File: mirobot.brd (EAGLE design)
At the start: 73.9 x 40.6 mm, 26 parts, among them IC1 ULN2003AN, IC2 ULN2003AN, IC3 ATMEGA 328, Q2 16M, X1 5_PIN_STEPPER, X2 5_PIN_STEPPER

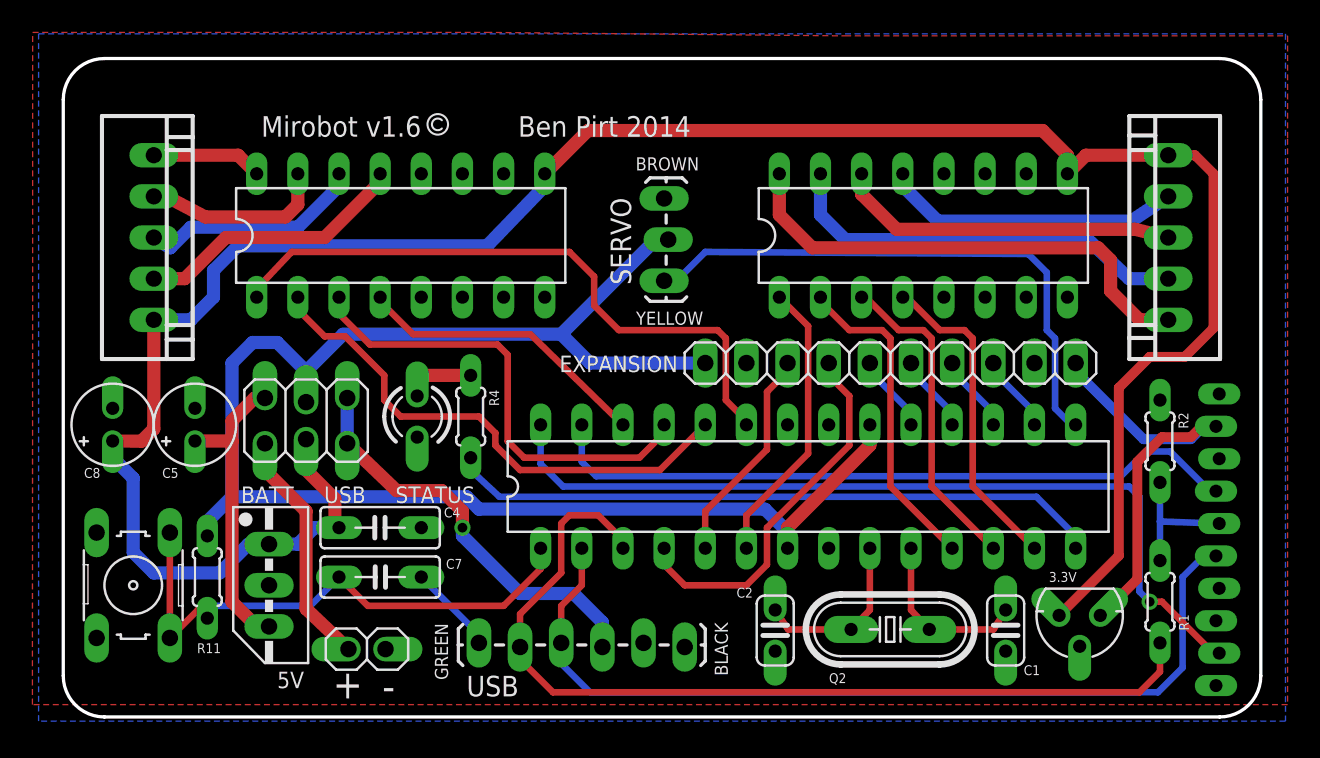
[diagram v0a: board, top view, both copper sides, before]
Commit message: Re-worked board to use the Arduino Pro Mini form factor
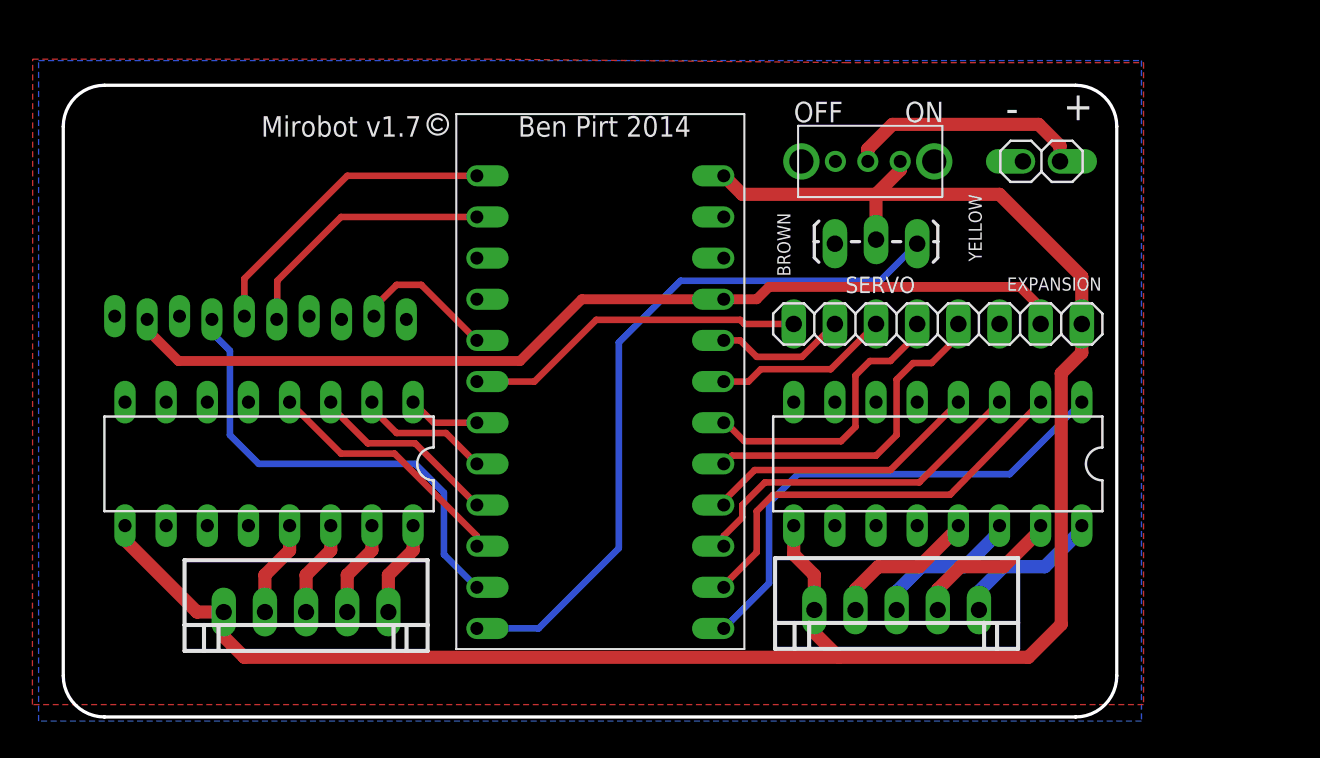
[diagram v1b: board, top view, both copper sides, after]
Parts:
- removed 3.3V: 3.3V, Child-Friendly-Parts:78LXX
- removed 5V: (no value), v-reg:78MXXS
- removed C1, C2: 22p, Child-Friendly-Parts:C025-024X044
- removed C4, C7: 100n, Child-Friendly-Parts:C050-025X075
- removed C5, C8: 100u, Child-Friendly-Parts:E2-5
- removed IC3: ATMEGA 328, atmel:DIL28-3
- removed JP5: PowerSelect, Child-Friendly-Parts:2X03
- removed Q2: 16M, Child-Friendly-Parts:HC49/S
- removed R1: 470R, Child-Friendly-Parts:0204/5
- removed R11: 10k, Child-Friendly-Parts:0204/5
- removed R2, R4: 1k, Child-Friendly-Parts:0204/5
- removed S1: Reset, switch-omron:B3F-10XX
- removed STATUS: (no value), Child-Friendly-Parts:LED3MM
- removed USB: (no value), SparkFun-Connectors:1X06_LOCK_LONGPADS
- added U$2: ARDUINO_PRO_MINI, custom:ARDUINO_PRO_MINI
- added U$3: SPDT_SLIDE_SWITCH, custom:SPDT_SLIDE_SWITCH
- EXPANSION: device pinhead:1X10 -> pinhead:1X08
- moved U$1 61.4 mm to (20.1, 40.4), turned to 0 degrees
- moved X2 58.0 mm to (23.9, 22.2), turned to 180 degrees
- moved JP6 51.4 mm to (69.3, 50.0), turned to 180 degrees
- moved X1 51.3 mm to (60.3, 22.4), turned to 180 degrees
- moved IC2 42.8 mm to (21.6, 31.4), turned to 180 degrees
- moved IC1 36.0 mm to (62.9, 31.4), turned to 180 degrees
- moved SERVO 15.8 mm to (61.6, 45.0), turned to 180 degrees
- moved EXPANSION 3.79 mm to (62.9, 40.0)
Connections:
- removed net +5V: EXPANSION.10, IC3.20, IC3.7, JP5.3, R11.2, SERVO.2
- removed net EXT_RESET: C4.2, USB.1
- removed net N$12: IC2.1, IC3.6
- removed net N$13: IC1.1, IC3.23
- removed net N$14: IC1.2, IC3.24
- removed net N$15: IC1.3, IC3.25
- removed net N$16: IC2.2, IC3.11
- removed net N$17: IC2.3, IC3.12
- removed net N$18: IC2.4, IC3.13
- removed net N$19: R1.2, R2.2, U$1.RX
- removed net N$20: R4.1, STATUS.A
- removed net N$5: IC1.4, IC3.26
- removed net N$7: C2.2, IC3.9, Q2.2
- removed net PB2: EXPANSION.3, IC3.16
- removed net PB3: EXPANSION.4, IC3.17
- removed net PB4: EXPANSION.5, IC3.18
- removed net PB5: EXPANSION.6, IC3.19
- removed net PD2: EXPANSION.7, IC3.4
- removed net RESET: C4.1, IC3.1, R11.1, S1.1, S1.2
- removed net STATUS: IC3.14, R4.2
- removed net USBVCC: JP5.1, JP5.2, USB.4
- removed net V+: 3.3V.IN, 5V.IN, C7.2, C8.+, IC1.9, IC2.9, JP5.4, X1.5, X2.5
- removed net VCC: 5V.OUT, C5.+, JP5.5
- new net MOTOR1_1: IC1.1, U$2.D10
- new net MOTOR1_2: IC1.2, U$2.MOSI
- new net MOTOR1_3: IC1.3, U$2.MISO
- new net MOTOR1_4: IC1.4, U$2.SCK
- new net MOTOR2_1: IC2.1, U$2.D4
- new net MOTOR2_2: IC2.2, U$2.D5
- new net MOTOR2_3: IC2.3, U$2.D6
- new net MOTOR2_4: IC2.4, U$2.D7
- new net PC0: EXPANSION.4, U$2.A0
- new net PC1: EXPANSION.5, U$2.A1
- new net PC2: EXPANSION.6, U$2.A2
- new net PC3: EXPANSION.7, U$2.A3
- net +3V3: now also EXPANSION.2, U$2.VCC; no longer 3.3V.OUT, EXPANSION.1
- net GND: now also EXPANSION.3, U$2.GND, U$2.GND2, U$3.GND1, U$3.GND2; no longer 3.3V.GND, 5V.GND, C1.1, C2.1, C5.-, C7.1, C8.-, EXPANSION.2, EXPANSION.9, IC3.22, IC3.8, R2.1, S1.3, S1.4, STATUS.K, USB.6
- net N$6: now also JP6.1, U$3.COMMON; no longer C1.2, IC3.10, Q2.1
- net NREADY: now also U$2.D2; no longer IC3.28
- net PD3: now also U$2.D3; no longer IC3.5
- net RXD: now also U$2.RXI; no longer IC3.2, USB.3
- net SERVO: now also U$2.D9; no longer IC3.15
- net TXD: now also U$1.RX, U$2.TXO; no longer IC3.3, R1.1, USB.2
- net VSS: now also EXPANSION.1, IC1.9, IC2.9, SERVO.2, U$2.RAW, U$3.SW2, X1.5, X2.5; no longer JP5.6, JP6.1
- net WIFI_RESET: now also U$2.D8; no longer IC3.27
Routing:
- net V+: track 144.6 -> 0.00 mm
- net VSS: track 14.9 -> 124.8 mm
- net +5V: track 100.3 -> 0.00 mm
- net NREADY: track 52.6 -> 8.88 mm, vias 1 -> 0
- net STATUS: track 40.5 -> 0.00 mm
- net N$13: track 39.6 -> 0.00 mm
- net RXD: track 55.7 -> 16.3 mm
- net TXD: track 57.2 -> 19.3 mm
- net RESET: track 34.5 -> 0.00 mm
- net N$14: track 32.5 -> 0.00 mm
- net +3V3: track 27.7 -> 60.0 mm
- net MOTOR1_1: track 0.00 -> 30.8 mm
- net N$15: track 29.0 -> 0.00 mm
- net MOTOR1_2: track 0.00 -> 25.9 mm
- net USBVCC: track 25.5 -> 0.00 mm, vias 1 -> 0
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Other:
- board size 73.9 x 40.6 mm -> 65 x 39 mm
- board text added: "Mirobot v1.7"
- board text added: "OFF"
- board text added: "ON"
- board text removed: "BATT"
- board text removed: "BLACK"
- board text removed: "GREEN"
- board text removed: "Mirobot v1.6"
- board text removed: "USB"

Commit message: Fully routed board to be used for the early bird units
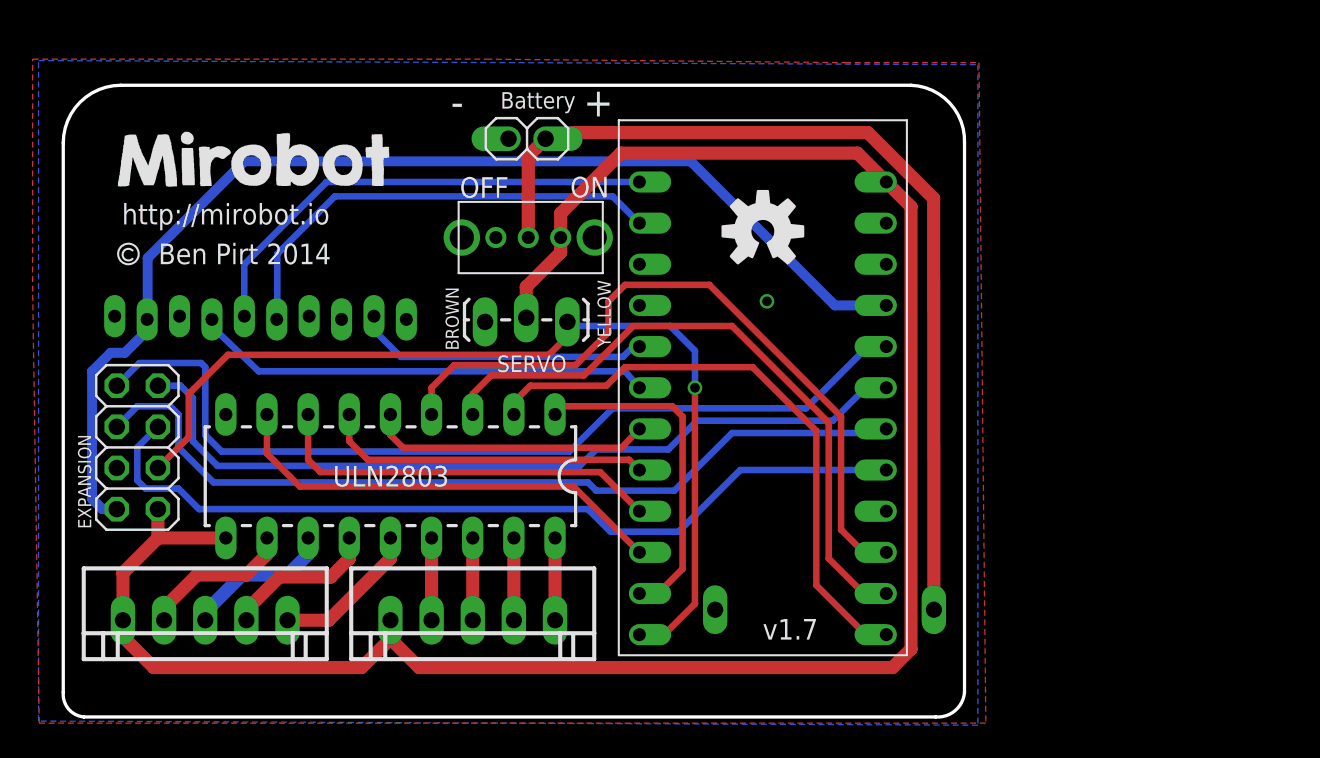
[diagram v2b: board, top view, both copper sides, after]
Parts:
- removed IC1, IC2: ULN2003AN, uln-udn:DIL16
- added LOGO1: OSHW-LOGOM, SparkFun-Aesthetics:OSHW-LOGO-M
- added U$4: BATTERY_PACK, custom:BATTERY_PACK
- added U$5: (no value), custom:LOGO
- added ULN2803: (no value), SparkFun-PowerIC:DIL18
- EXPANSION: device pinhead:1X08 -> pinhead:2X04
- moved EXPANSION 50.0 mm to (13.5, 32.4), turned to 90 degrees
- moved JP6 31.8 mm to (37.5, 51.4)
- moved X1 26.2 mm to (34.2, 21.7)
- moved SERVO 22.1 mm to (40.0, 40.1)
- moved U$3 21.5 mm to (37.6, 45.3)
- moved U$2 10.0 mm to (52.1, 36.1)
- moved X2 6.24 mm to (17.7, 21.7)
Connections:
- removed net N$10: IC2.14, X2.3
- removed net N$11: IC2.13, X2.4
- removed net PD3: EXPANSION.8, U$2.D3
- new net N$5: ULN2803.14, X2.1
- new net N$7: ULN2803.13, X2.2
- net GND: now also EXPANSION.4, U$4.GND, ULN2803.9; no longer EXPANSION.3, IC1.5, IC1.6, IC1.7, IC1.8, IC2.5, IC2.6, IC2.7, IC2.8
- net MOTOR1_1: now also U$2.D8, ULN2803.1; no longer IC1.1, U$2.D10
- net MOTOR1_2: now also U$2.D10, ULN2803.2; no longer IC1.2, U$2.MOSI
- net MOTOR1_3: now also U$2.MOSI, ULN2803.3; no longer IC1.3, U$2.MISO
- net MOTOR1_4: now also U$2.MISO, ULN2803.4; no longer IC1.4, U$2.SCK
- net MOTOR2_1: now also ULN2803.5; no longer IC2.1
- net MOTOR2_2: now also ULN2803.6; no longer IC2.2
- net MOTOR2_3: now also ULN2803.7; no longer IC2.3
- net MOTOR2_4: now also ULN2803.8; no longer IC2.4
- net N$1: now also ULN2803.18; no longer IC1.16
- net N$2: now also ULN2803.17; no longer IC1.15
- net N$3: now also ULN2803.16; no longer IC1.14
- net N$4: now also ULN2803.15; no longer IC1.13
- net N$6: now also U$4.VSS
- net N$8: now also ULN2803.12, X2.3; no longer IC2.16, X2.1
- net N$9: now also ULN2803.11, X2.4; no longer IC2.15, X2.2
- net PC0: now also EXPANSION.5; no longer EXPANSION.4
- net PC1: now also EXPANSION.6; no longer EXPANSION.5
- net PC2: now also EXPANSION.7; no longer EXPANSION.6
- net PC3: now also EXPANSION.8; no longer EXPANSION.7
- net SERVO: now also EXPANSION.3
- net VSS: now also ULN2803.10; no longer IC1.9, IC2.9
- net WIFI_RESET: now also U$2.D3; no longer U$2.D8
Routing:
- net PC3: track 8.12 -> 55.5 mm
- net N$6: track 14.8 -> 57.8 mm
- net PC2: track 10.9 -> 50.6 mm
- net PC1: track 17.6 -> 52.9 mm
- net PC0: track 20.5 -> 52.9 mm
- net MOTOR1_4: track 17.3 -> 44.4 mm
- net PD3: track 21.2 -> 0.00 mm
- net MOTOR1_3: track 21.5 -> 40.3 mm
- net SERVO: track 44.5 -> 59.5 mm, vias 0 -> 1
- net MOTOR2_1: track 4.46 -> 17.5 mm
- net MOTOR2_3: track 11.8 -> 24.6 mm
- net MOTOR2_4: track 15.6 -> 27.9 mm
- net RXD: track 16.3 -> 28.6 mm
- net MOTOR2_2: track 8.28 -> 20.3 mm
- net MOTOR1_2: track 25.9 -> 37.1 mm
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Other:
- board size 65 x 39 mm -> 55.6 x 39 mm
- board text added: "http://mirobot.io"
- board text added: "v1.7"
- board text removed: "Mirobot v1.7"

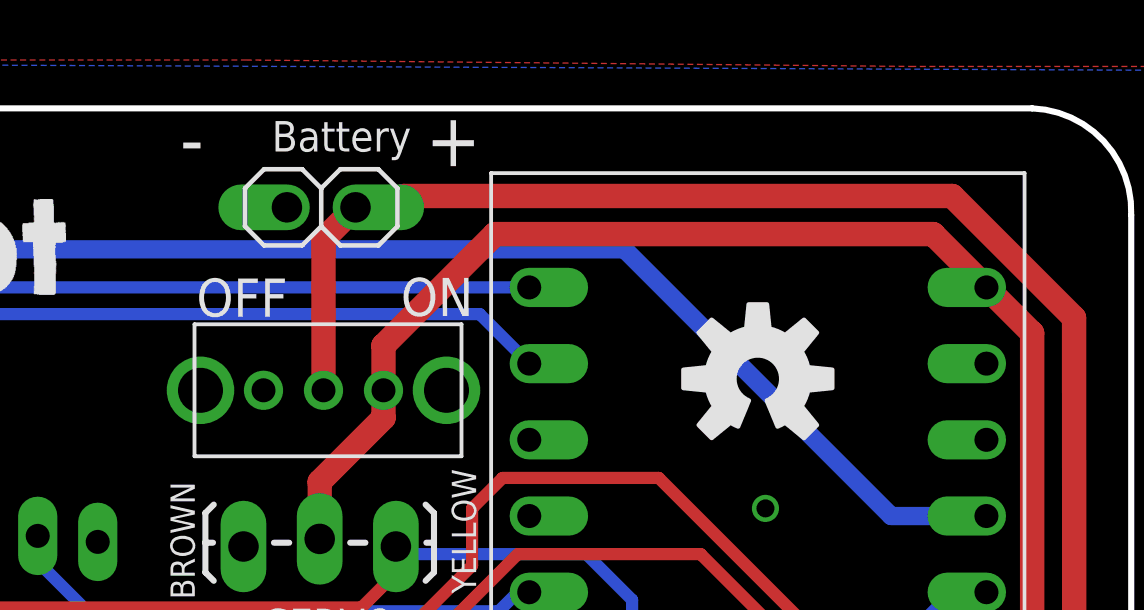
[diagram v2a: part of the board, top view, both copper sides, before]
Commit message: Remove the extra power pins and make the switch easier to solder
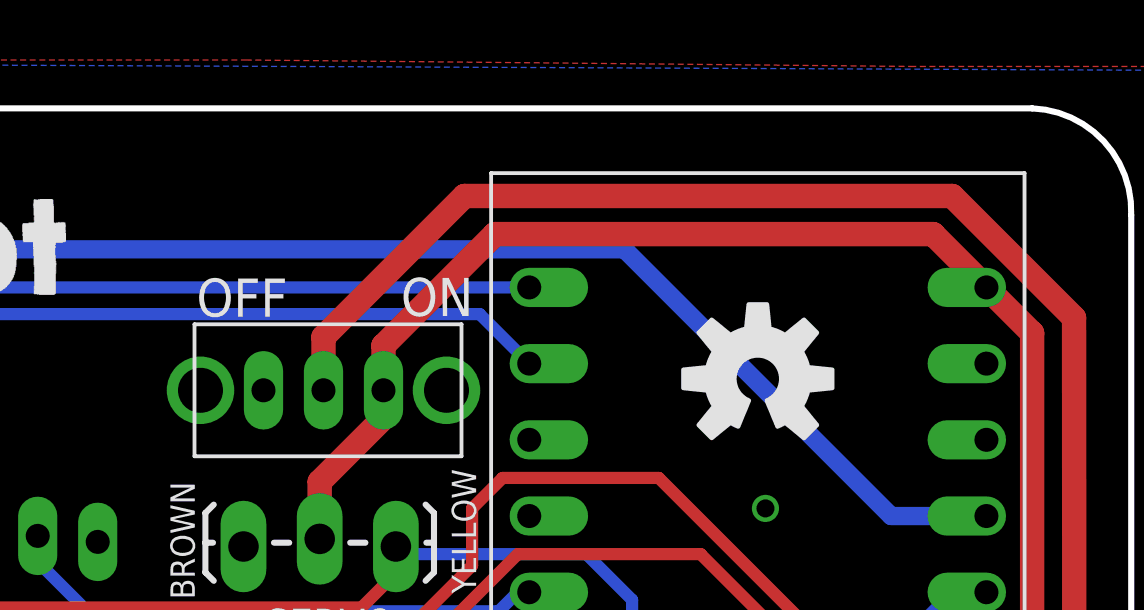
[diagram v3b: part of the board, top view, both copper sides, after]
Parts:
- removed JP6: Battery, Child-Friendly-Parts:1X02
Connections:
- net GND: no longer JP6.2
- net N$6: no longer JP6.1
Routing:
- net N$6: track 57.8 -> 55.8 mm
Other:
- board text removed: "+"
- board text removed: "-"
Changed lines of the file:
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@@
 <board>
 <plain>
-<text x="40.999740625" y="52.81104375" size="1.778" layer="25">+</text>
-<text x="32.808821875" y="52.832153125" size="1.778" layer="25">-</text>
 <text x="52.059153125" y="20.524040625" size="1.27" layer="25">v1.7</text>
 <text x="14.757203125" y="43.693228125" size="1.27" layer="25">Ben Pirt 2014</text>
@@
 </autorouter>
 <elements>
-<element name="JP6" library="Child-Friendly-Parts" package="1X02" value="Battery" x="37.516" y="51.438" smashed="yes" rot="R180">
-<attribute name="VALUE" x="40.51279375" y="54.313684375" size="1.016" layer="21" rot="R180"/>
-</element>
 <element name="X1" library="custom" package="5_PIN_STEPPER" value="5_PIN_STEPPER" x="34.163" y="21.717" smashed="yes" rot="R180">
 <attribute name="OC_NEWARK" value="38C9178" x="34.163" y="21.717" size="1.778" layer="27" rot="R180" display="off"/>
@@
 <signals>
 <signal name="GND">
-<contactref element="JP6" pad="2"/>
 <polygon width="0.2" layer="1" isolate="0.254">
 <vertex x="7" y="56.349"/>
@@
 <contactref element="U$2" pad="GND"/>
 <contactref element="U$2" pad="GND2"/>
-<contactref element="U$3" pad="GND1"/>
-<contactref element="U$3" pad="GND2"/>
 <contactref element="ULN2803" pad="9"/>
 <contactref element="EXPANSION" pad="4"/>
 <via x="52.324" y="41.402" extent="1-16" drill="0.6" shape="octagon"/>
 <contactref element="U$4" pad="GND"/>
+<contactref element="U$3" pad="GND1"/>
+<contactref element="U$3" pad="GND2"/>
 </signal>
 <signal name="SERVO">
@@
 <signal name="N$6">
 <contactref element="U$3" pad="COMMON"/>
-<contactref element="JP6" pad="1"/>
-<wire x1="38.659" y1="51.438" x2="37.592" y2="50.371" width="0.8128" layer="1"/>
-<wire x1="37.592" y1="50.371" x2="37.592" y2="45.339" width="0.8128" layer="1"/>
 <contactref element="U$4" pad="VSS"/>
 <wire x1="62.627" y1="22.368" x2="62.611" y2="47.752" width="0.8128" layer="1"/>
 <wire x1="62.611" y1="47.752" x2="58.547" y2="51.816" width="0.8128" layer="1"/>
-<wire x1="58.547" y1="51.816" x2="40.259" y2="51.816" width="0.8128" layer="1"/>
-<wire x1="40.259" y1="51.816" x2="40.132" y2="51.435" width="0.8128" layer="1"/>
-<wire x1="40.132" y1="51.435" x2="38.662" y2="51.435" width="0.8128" layer="1"/>
-<wire x1="38.662" y1="51.435" x2="38.659" y2="51.438" width="0.8128" layer="1"/>
+<wire x1="58.547" y1="51.816" x2="42.291" y2="51.816" width="0.8128" layer="1"/>
+<wire x1="42.291" y1="51.816" x2="37.592" y2="47.117" width="0.8128" layer="1"/>
+<wire x1="37.592" y1="47.117" x2="37.592" y2="45.339" width="0.8128" layer="1"/>
 </signal>
 <signal name="N$1">

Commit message: v1.8 boards
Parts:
- removed EXPANSION: (no value), pinhead:2X04
- removed SERVO: (no value), SparkFun-Connectors:1X03_LOCK_LONGPADS
- added BUMP, LINE: (no value), Child-Friendly-Parts:1X04
- added PEN: (no value), SparkFun-Connectors:1X03_LOCK_LONGPADS
- added SOUND: (no value), pinhead:1X02
- moved U$5 32.0 mm to (52.5, 50.7)
- moved U$1 31.8 mm to (51.8, 42.3)
- moved U$2 28.7 mm to (24.8, 45.0), turned to 90 degrees
- moved U$3 27.8 mm to (52.1, 21.6)
- moved LOGO1 26.7 mm to (25.4, 45.0)
- moved U$4 3.81 mm to (59.8, 23.4)
- moved ULN2803 3.05 mm to (26.0, 30.6)
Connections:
- removed net WIFI_RESET: U$1.EXT_RESET, U$2.D3
- new net SPEAKER: SOUND.2, U$2.D9
- net +3V3: now also BUMP.3, LINE.3; no longer EXPANSION.2
- net GND: now also BUMP.4, LINE.4, PEN.3, SOUND.1; no longer EXPANSION.4, SERVO.3
- net PC0: now also LINE.2; no longer EXPANSION.5
- net PC1: now also LINE.1; no longer EXPANSION.6
- net PC2: now also BUMP.2; no longer EXPANSION.7
- net PC3: now also BUMP.1; no longer EXPANSION.8
- net SERVO: now also PEN.1, U$2.D3; no longer EXPANSION.3, SERVO.1, U$2.D9
- net VSS: now also PEN.2; no longer EXPANSION.1, SERVO.2
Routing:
- net N$6: track 55.8 -> 10.0 mm
- net SERVO: track 59.5 -> 29.1 mm, vias 1 -> 0
- net VSS: track 124.6 -> 94.4 mm
- net NREADY: track 18.4 -> 47.7 mm, vias 0 -> 2
- net WIFI_RESET: track 28.4 -> 0.00 mm
- net MOTOR1_4: track 44.4 -> 20.8 mm
- net RXD: track 28.6 -> 50.2 mm, vias 0 -> 1
- net TXD: track 29.7 -> 50.9 mm, vias 0 -> 1
- net MOTOR1_3: track 40.3 -> 20.8 mm
- net MOTOR1_1: track 21.3 -> 3.45 mm
- net PC1: track 52.9 -> 35.6 mm
- net PC0: track 52.9 -> 36.3 mm
- net MOTOR1_2: track 37.1 -> 20.8 mm
- net MOTOR2_1: track 17.5 -> 3.45 mm
- net PC3: track 55.5 -> 43.3 mm
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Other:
- board text added: "GND"
- board text added: "v1.8"
- board text removed: "v1.7"
